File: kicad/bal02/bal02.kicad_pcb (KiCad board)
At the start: 2 copper layers, 4 parts, among them IC1 nucleo32-L432, IC2 nRF24L01_SMD_MODULE, IC3 MPU9250_SMD_MODULE

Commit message: more components added
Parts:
- added C3: 100uF/25V, bal:WCAP-ATG8, F.Cu at (106.0, 53.9)
- added C4: 100uF/25V, bal:WCAP-ATG8, F.Cu at (113.5, 53.9)
- added D2: 1N4148WT, Diode_SMD:D_SOD-523, F.Cu at (119.1, 50.2)
- added D3: 1N4148WT, Diode_SMD:D_SOD-523, F.Cu at (119.1, 52.7)
- added IC4: M24C16-FMN6TP, bal:SOIC127P600X175-8N, F.Cu at (106.5, 61.3)
- added IC5: SN65HVD230DR, bal:SOT127P600X175-8N, F.Cu at (115.0, 61.4)
- added IC6: TLV76050DBZR, bal:SOT95P237X112-3N, F.Cu at (104.8, 66.9)
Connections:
- IC2 pad 6: nRF_MOSI -> Net-(IC2-MOSI)
- IC2 pad 7: nRF_MISO -> Net-(IC2-MISO)
- IC3 pad 4: unconnected-(IC3-SDA-Pad4) -> Net-(IC3-SDA)
- IC3 pad 7: unconnected-(IC3-AD0-Pad7) -> Net-(IC3-AD0)

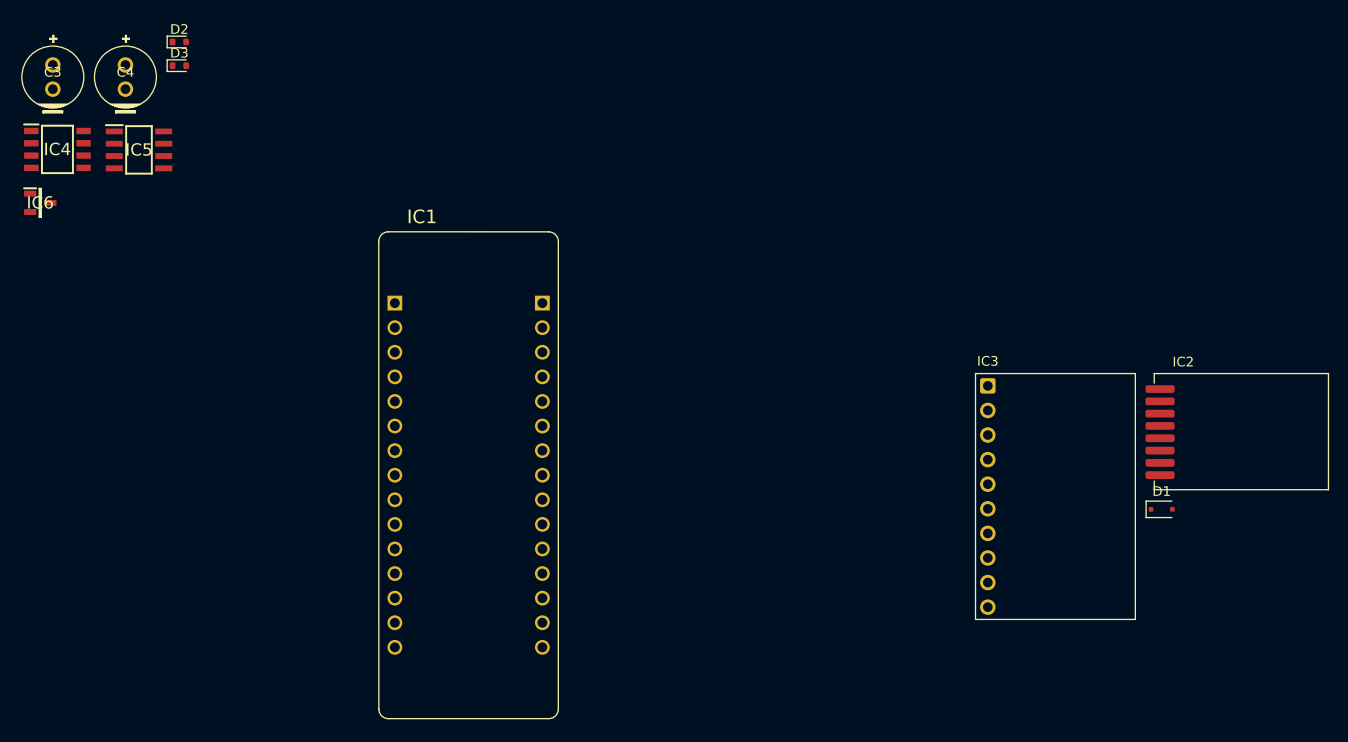
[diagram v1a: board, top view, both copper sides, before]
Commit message: bal02 placement + nucleo32 update
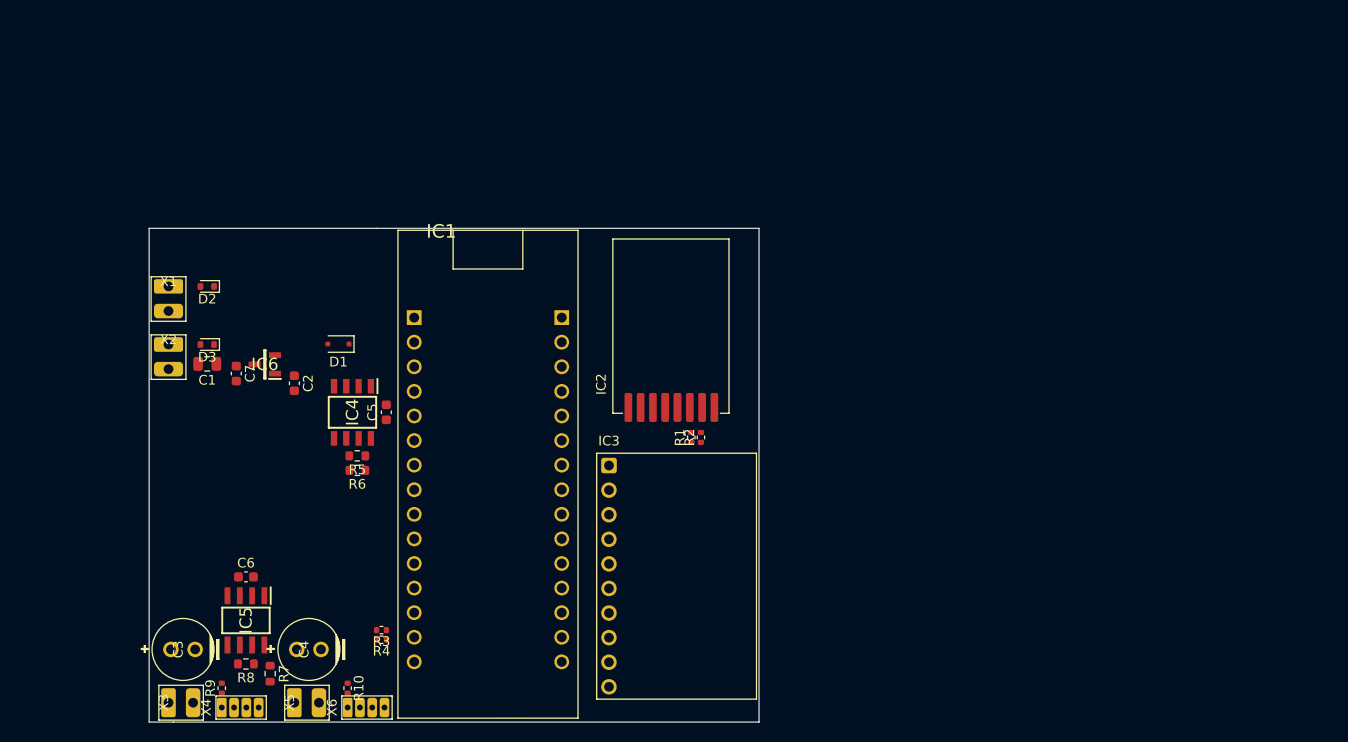
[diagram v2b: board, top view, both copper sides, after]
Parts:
- added C1: 10uF, Capacitor_SMD:C_0805_2012Metric, F.Cu at (122.0, 83.5)
- added C2: 100nF, Capacitor_SMD:C_0603_1608Metric, F.Cu at (131.0, 85.5)
- added C5: 100nF, Capacitor_SMD:C_0603_1608Metric, F.Cu at (140.5, 88.5)
- added C6: 100nF, Capacitor_SMD:C_0603_1608Metric, F.Cu at (126.0, 105.5)
- added C7: 100nF, Capacitor_SMD:C_0603_1608Metric, F.Cu at (125.0, 84.5)
- added R1: R, Resistor_SMD:R_0402_1005Metric, F.Cu at (172.0, 91.1)
- added R10: R, Resistor_SMD:R_0402_1005Metric, F.Cu at (136.5, 117.0)
- added R2: R, Resistor_SMD:R_0402_1005Metric, F.Cu at (173.0, 91.1)
- added R3: R, Resistor_SMD:R_0402_1005Metric, F.Cu at (140.0, 111.0)
- added R4: R, Resistor_SMD:R_0402_1005Metric, F.Cu at (140.0, 112.0)
- added R5: 4k7, Resistor_SMD:R_0603_1608Metric, F.Cu at (137.5, 93.0)
- added R6: 4k7, Resistor_SMD:R_0603_1608Metric, F.Cu at (137.5, 94.5)
- added R7: 0R, Resistor_SMD:R_0603_1608Metric, F.Cu at (128.5, 115.5)
- added R8: 120R, Resistor_SMD:R_0603_1608Metric, F.Cu at (126.0, 114.5)
- added R9: R, Resistor_SMD:R_0402_1005Metric, F.Cu at (123.5, 117.0)
- added X1: ~, bal:H2_100mil, F.Cu at (118.0, 75.5)
- added X2: ~, bal:H2_100mil, F.Cu at (118.0, 81.5)
- added X3: ~, bal:H2_100mil, F.Cu at (118.0, 118.5)
- added X4: ~, bal:H4_50mil, F.Cu at (123.5, 119.0)
- added X5: ~, bal:H2_100mil, F.Cu at (131.0, 118.5)
- added X6: ~, bal:H4_50mil, F.Cu at (136.5, 119.0)
- moved D1 86.7 mm to (135.6, 81.5), turned to 180 degrees
- moved C4 62.1 mm to (132.5, 113.0), turned to 90 degrees
- moved C3 60.6 mm to (119.5, 113.0), turned to 90 degrees
- moved IC2 54.4 mm to (165.5, 88.6), turned to 90 degrees
- moved IC5 49.8 mm to (126.0, 110.0), turned to -90 degrees
- moved IC4 40.8 mm to (137.0, 88.5), turned to -90 degrees
- moved IC3 40.0 mm to (163.5, 94.0)
- moved D3 28.9 mm to (122.0, 81.5), turned to 180 degrees
- moved IC6 28.6 mm to (128.0, 83.5), turned to 180 degrees
- moved D2 25.4 mm to (122.0, 75.5), turned to 180 degrees
- moved IC1 2.50 mm to (151.0, 96.5)
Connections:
- net Net-(D2-K) renamed +BATT
- D2 pad 2: unconnected-(D2-A-Pad2) -> Net-(D2-A)
- D3 pad 2: unconnected-(D3-A-Pad2) -> Net-(D3-A)
- IC5 pad 1: unconnected-(IC5-D-Pad1) -> CAN_TX
- IC5 pad 2: unconnected-(IC5-GND-Pad2) -> GND
- IC5 pad 3: unconnected-(IC5-VCC-Pad3) -> +3V3
- IC5 pad 4: unconnected-(IC5-R-Pad4) -> CAN_RX
- IC5 pad 6: unconnected-(IC5-CANL-Pad6) -> Net-(IC5-CANL)
- IC5 pad 7: unconnected-(IC5-CANH-Pad7) -> Net-(IC5-CANH)
- IC5 pad 8: unconnected-(IC5-RS-Pad8) -> Net-(IC5-RS)
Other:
- board outline added: 63 x 51 mm

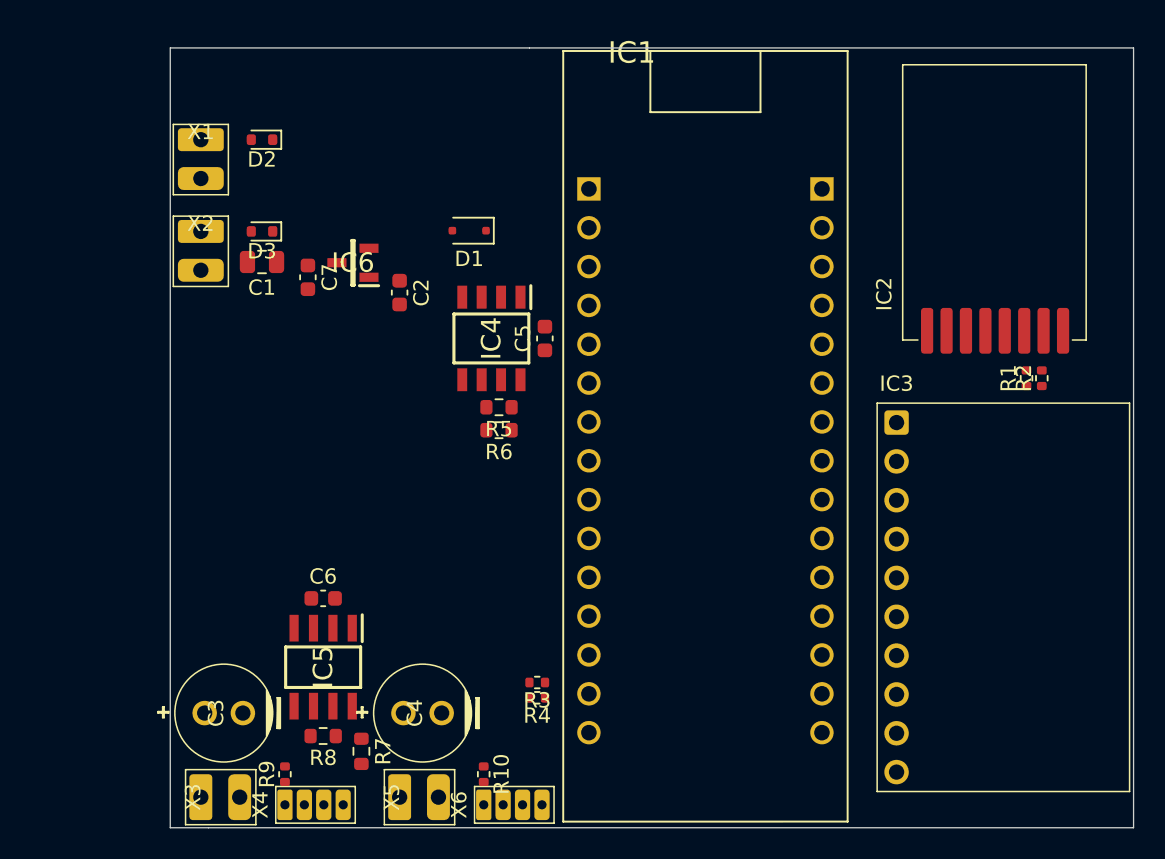
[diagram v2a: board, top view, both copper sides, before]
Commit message: bal01 replaced sensor using MA702GQ
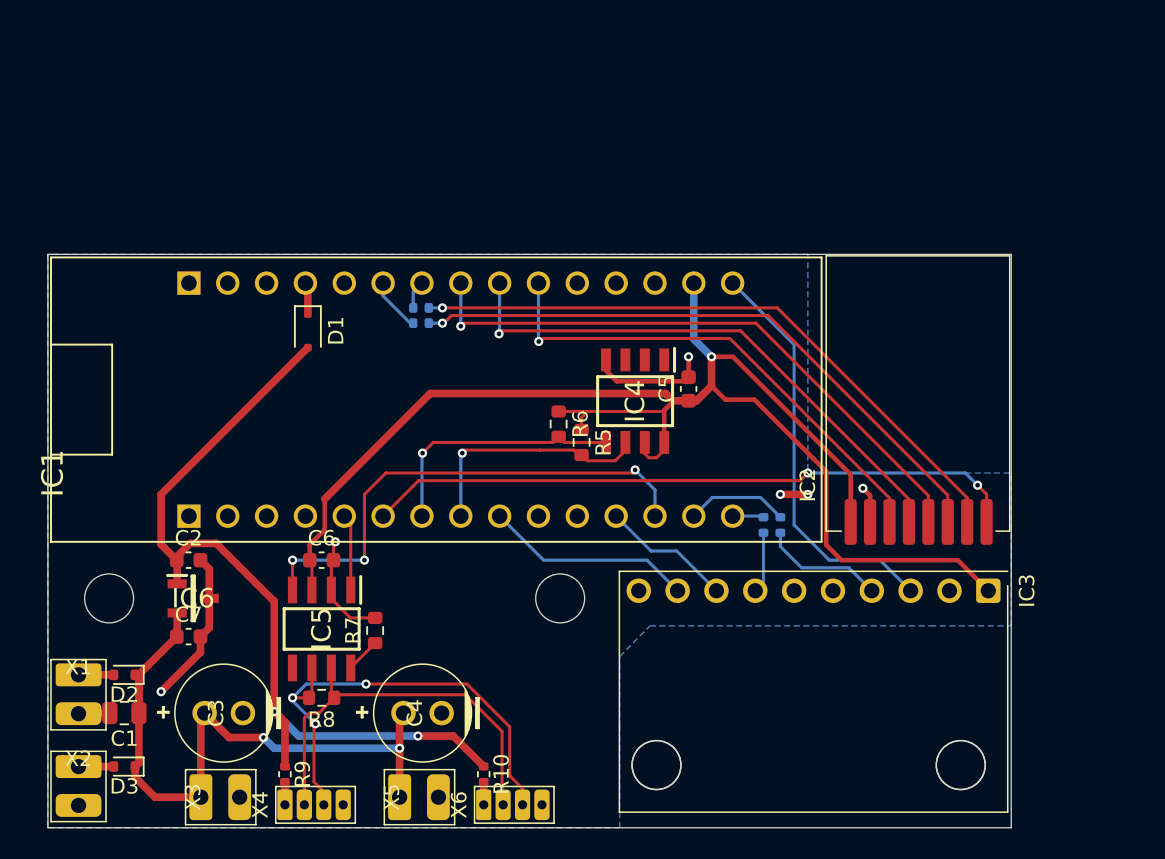
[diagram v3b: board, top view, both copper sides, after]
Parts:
- R1, R2, R3, R4: moved to B.Cu
- moved R2 40.9 mm to (132.4, 86.5), turned to 0 degrees
- moved R1 39.8 mm to (132.4, 87.5), turned to 0 degrees
- moved D2 36.1 mm to (113.0, 110.5)
- moved D3 36.1 mm to (113.0, 116.5)
- moved X1 35.9 mm to (110.0, 110.5)
- moved X2 35.9 mm to (110.0, 116.5)
- moved C1 30.8 mm to (113.0, 113.0)
- moved C7 24.8 mm to (117.2, 108.0), turned to 0 degrees
- moved IC6 24.3 mm to (117.5, 105.5), turned to 0 degrees
- moved C2 22.3 mm to (117.2, 103.0), turned to 0 degrees
- moved R3 18.9 mm to (155.9, 100.7), turned to -90 degrees
- moved R4 18.6 mm to (154.8, 100.7), turned to -90 degrees
- moved IC1 16.5 mm to (135.0, 92.5), turned to 90 degrees
- moved IC2 13.5 mm to (160.5, 101.1)
- moved IC3 12.5 mm to (169.5, 105.0), turned to -90 degrees
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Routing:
- net +3V3: track 0.00 -> 98.3 mm, vias 0 -> 1
- net +5V: track 0.00 -> 54.7 mm, vias 0 -> 2
- net +BATT: track 0.00 -> 44.2 mm, vias 0 -> 2
- net nRF_IRQ: track 0.00 -> 43.0 mm, vias 0 -> 2
- net Net-(IC2-MISO): track 0.00 -> 41.9 mm, vias 0 -> 1
- net Net-(IC2-MOSI): track 0.00 -> 40.8 mm, vias 0 -> 1
- net nRF_SCK: track 0.00 -> 39.9 mm, vias 0 -> 1
- net nRF_CS: track 0.00 -> 36.3 mm, vias 0 -> 1
- net CAN_RX: track 0.00 -> 32.9 mm, vias 0 -> 3
- net nRF_CE: track 0.00 -> 32.7 mm, vias 0 -> 1
- net Net-(IC5-CANL): track 0.00 -> 32.6 mm, vias 0 -> 3
- net GND: track 0.00 -> 32.0 mm, vias 0 -> 6
- net Net-(IC5-CANH): track 0.00 -> 27.1 mm
- net ACC_SCK: track 0.00 -> 26.9 mm
- net I2C1_SDA: track 0.00 -> 16.7 mm, vias 0 -> 1
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- added copper zone on B.Cu, net GND
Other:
- board size 63 x 51 mm -> 63 x 37.5 mm
